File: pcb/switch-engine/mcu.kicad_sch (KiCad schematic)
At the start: 78 parts, among them J10 CORTEX_DEBUG_ETM, J12 CONN_01X03, J13 PMOD_HOST, J26 RJ45, J9 PMOD_HOST, U14 ECS-1612MV-250-CN, U17 AT24MAC402, U29 ADM3101E_QFN, U8 XCKU5P-2FFVB676I, U9 STM32H735-UFBGA176-25

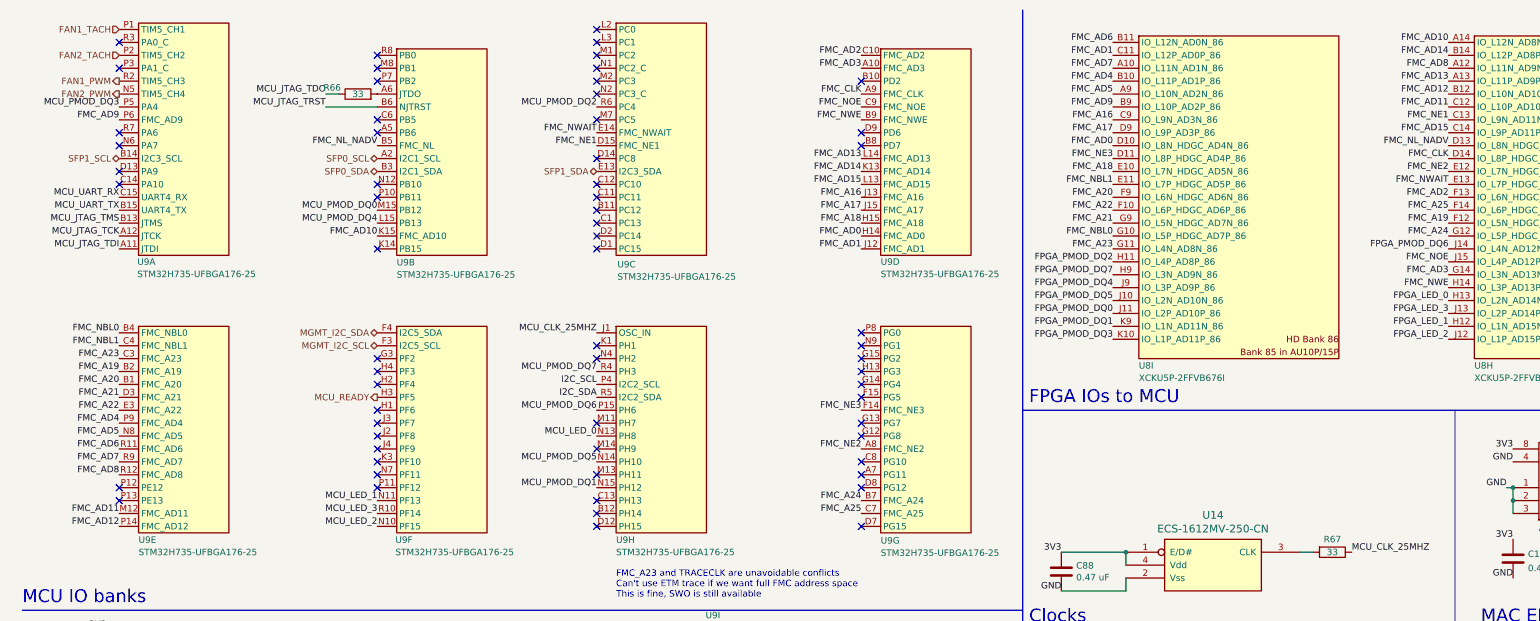
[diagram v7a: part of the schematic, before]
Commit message: Continued layout of MCU area, added cutout for fan
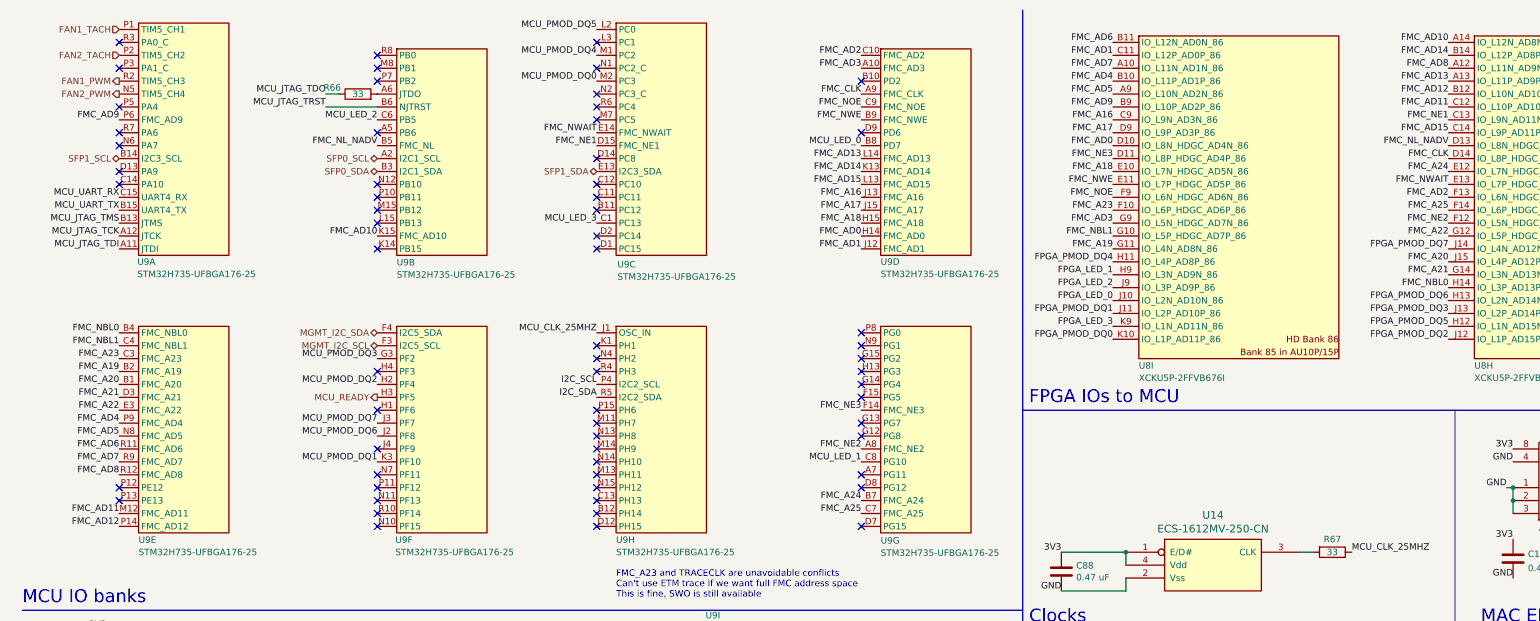
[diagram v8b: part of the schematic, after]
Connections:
- net FMC_A19: now also U8.G11 (IO_L4N_AD8N_86); no longer U8.F12 (IO_L5N_HDGC_87)
- net FMC_A20: now also U8.J15 (IO_L4P_AD12P_87); no longer U8.F9 (IO_L6N_HDGC_AD6N_86)
- net FMC_A21: now also U8.G14 (IO_L3N_AD13N_87); no longer U8.G9 (IO_L5N_HDGC_AD7N_86)
- net FMC_A22: now also U8.G12 (IO_L5P_HDGC_87); no longer U8.F10 (IO_L6P_HDGC_AD6P_86)
- net FMC_A23: now also U8.F10 (IO_L6P_HDGC_AD6P_86); no longer U8.G11 (IO_L4N_AD8N_86)
- net FMC_A24: now also U8.E12 (IO_L7N_HDGC_87); no longer U8.G12 (IO_L5P_HDGC_87)
- net FMC_AD3: now also U8.G9 (IO_L5N_HDGC_AD7N_86); no longer U8.G14 (IO_L3N_AD13N_87)
- net FMC_NBL0: now also U8.H14 (IO_L3P_AD13P_87); no longer U8.G10 (IO_L5P_HDGC_AD7P_86)
- net FMC_NBL1: now also U8.G10 (IO_L5P_HDGC_AD7P_86); no longer U8.E11 (IO_L7P_HDGC_AD5P_86)
- net FMC_NE2: now also U8.F12 (IO_L5N_HDGC_87); no longer U8.E12 (IO_L7N_HDGC_87)
- net FMC_NOE: now also U8.F9 (IO_L6N_HDGC_AD6N_86); no longer U8.J15 (IO_L4P_AD12P_87)
- net FMC_NWE: now also U8.E11 (IO_L7P_HDGC_AD5P_86); no longer U8.H14 (IO_L3P_AD13P_87)
- net FPGA_LED_0: now also U8.J10 (IO_L2N_AD10N_86); no longer U8.H13 (IO_L2N_AD14N_87)
- net FPGA_LED_1: now also U8.H9 (IO_L3N_AD9N_86); no longer U8.H12 (IO_L1N_AD15N_87)
- net FPGA_LED_2: now also U8.J9 (IO_L3P_AD9P_86); no longer U8.J12 (IO_L1P_AD15P_87)
- net FPGA_LED_3: now also U8.K9 (IO_L1N_AD11N_86); no longer U8.J13 (IO_L2P_AD14P_87)
- net FPGA_PMOD_DQ0: now also U8.K10 (IO_L1P_AD11P_86); no longer U8.J11 (IO_L2P_AD10P_86)
- net FPGA_PMOD_DQ1: now also U8.J11 (IO_L2P_AD10P_86); no longer U8.K9 (IO_L1N_AD11N_86)
- net FPGA_PMOD_DQ2: now also U8.J12 (IO_L1P_AD15P_87); no longer U8.H11 (IO_L4P_AD8P_86)
- net FPGA_PMOD_DQ3: now also U8.J13 (IO_L2P_AD14P_87); no longer U8.K10 (IO_L1P_AD11P_86)
- net FPGA_PMOD_DQ4: now also U8.H11 (IO_L4P_AD8P_86); no longer U8.J9 (IO_L3P_AD9P_86)
- net FPGA_PMOD_DQ5: now also U8.H12 (IO_L1N_AD15N_87); no longer U8.J10 (IO_L2N_AD10N_86)
- net FPGA_PMOD_DQ6: now also U8.H13 (IO_L2N_AD14N_87); no longer U8.J14 (IO_L4N_AD12N_87)
- net FPGA_PMOD_DQ7: now also U8.J14 (IO_L4N_AD12N_87); no longer U8.H9 (IO_L3N_AD9N_86)
- net MCU_LED_0: now also U9.B8 (PD7); no longer U9.N13 (PH8)
- net MCU_LED_1: now also U9.C8 (PG10); no longer U9.N11 (PF13)
- net MCU_LED_2: now also U9.C6 (PB5); no longer U9.N10 (PF15)
- net MCU_LED_3: now also U9.C1 (PC13); no longer U9.R10 (PF14)
- net MCU_PMOD_DQ0: now also U9.M2 (PC3); no longer U9.M15 (PB12)
- net MCU_PMOD_DQ1: now also U9.K3 (PF10); no longer U9.N15 (PH12)
- net MCU_PMOD_DQ2: now also U9.H2 (PF4); no longer U9.R6 (PC4)
- net MCU_PMOD_DQ3: now also U9.G3 (PF2); no longer U9.P5 (PA4)
- net MCU_PMOD_DQ4: now also U9.M1 (PC2); no longer U9.L15 (PB13)
- net MCU_PMOD_DQ5: now also U9.L2 (PC0); no longer U9.N14 (PH10)
- net MCU_PMOD_DQ6: now also U9.J2 (PF8); no longer U9.P15 (PH6)
- net MCU_PMOD_DQ7: now also U9.J3 (PF7); no longer U9.R4 (PH3)
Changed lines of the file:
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@@
 	(title_block
 		(title "LATENTRED Ethernet Switch - Main Board")
-		(date "2025-06-04")
+		(date "2025-06-06")
 		(rev "0.1")
 		(company "Antikernel Labs")
@@
 	)
 	(no_connect
-		(at 127 109.22)
+		(at 127 31.75)
 	)
 	(no_connect
-		(at 127 54.61)
+		(at 127 109.22)
 	)
 	(no_connect
@@
 	)
 	(no_connect
-		(at 179.07 101.6)
+		(at 33.02 31.75)
+	)
+	(no_connect
+		(at 127 83.82)
 	)
 	(no_connect
@@
 	)
 	(no_connect
-		(at 83.82 93.98)
-	)
-	(no_connect
 		(at 179.07 114.3)
 	)
@@
 	)
 	(no_connect
-		(at 179.07 39.37)
+		(at 127 96.52)
 	)
 	(no_connect
@@
 	)
 	(no_connect
-		(at 83.82 86.36)
+		(at 83.82 111.76)
+	)
+	(no_connect
+		(at 127 106.68)
 	)
 	(no_connect
@@
 	)
 	(no_connect
-		(at 179.07 86.36)
+		(at 83.82 109.22)
 	)
 	(no_connect
-		(at 83.82 59.69)
+		(at 179.07 86.36)
 	)
 	(no_connect
-		(at 83.82 34.29)
+		(at 83.82 59.69)
 	)
 	(no_connect
@@
 	)
 	(no_connect
-		(at 83.82 81.28)
+		(at 83.82 91.44)
 	)
 	(no_connect
-		(at 127 21.59)
+		(at 179.07 96.52)
 	)
 	(no_connect
-		(at 83.82 91.44)
+		(at 127 101.6)
 	)
 	(no_connect
-		(at 179.07 96.52)
+		(at 83.82 114.3)
 	)
 	(no_connect
@@
 	)
 	(no_connect
+		(at 83.82 54.61)
+	)
+	(no_connect
+		(at 83.82 52.07)
+	)
+	(no_connect
 		(at 127 57.15)
 	)
@@
 	)
 	(no_connect
-		(at 83.82 101.6)
-	)
-	(no_connect
 		(at 83.82 46.99)
 	)
 	(no_connect
-		(at 127 26.67)
-	)
-	(no_connect
 		(at 179.07 81.28)
 	)
@@
 	)
 	(no_connect
+		(at 127 91.44)
+	)
+	(no_connect
 		(at 27.94 261.62)
 	)
@@
 	)
 	(no_connect
-		(at 83.82 96.52)
-	)
-	(no_connect
 		(at 83.82 49.53)
 	)
@@
 	)
 	(no_connect
-		(at 127 16.51)
-	)
-	(no_connect
 		(at 179.07 88.9)
 	)
@@
 	)
 	(label "FPGA_PMOD_DQ6"
-		(at 294.64 59.69 180)
+		(at 294.64 69.85 180)
 		(fields_autoplaced yes)
 		(effects
@@
 	)
 	(label "FMC_AD3"
-		(at 294.64 64.77 180)
+		(at 228.6 54.61 180)
 		(fields_autoplaced yes)
 		(effects
@@
 	)
 	(label "FMC_NWE"
-		(at 294.64 67.31 180)
+		(at 228.6 46.99 180)
 		(fields_autoplaced yes)
 		(effects
@@
 	)
 	(label "MCU_LED_2"
-		(at 83.82 114.3 180)
+		(at 83.82 34.29 180)
 		(fields_autoplaced yes)
 		(effects
@@
 	)
 	(label "MCU_LED_1"
-		(at 83.82 109.22 180)
+		(at 179.07 101.6 180)
 		(fields_autoplaced yes)
 		(effects
@@
 	)
 	(label "FMC_NBL1"
-		(at 228.6 46.99 180)
+		(at 228.6 57.15 180)
 		(fields_autoplaced yes)
 		(effects
@@
 	)
 	(label "FPGA_PMOD_DQ4"
-		(at 228.6 67.31 180)
+		(at 228.6 62.23 180)
 		(fields_autoplaced yes)
 		(effects
@@
 	)
 	(label "FPGA_LED_0"
-		(at 294.64 69.85 180)
+		(at 228.6 69.85 180)
 		(fields_autoplaced yes)
 		(effects
@@
 	)
 	(label "MCU_LED_3"
-		(at 83.82 111.76 180)
+		(at 127 54.61 180)
 		(fields_autoplaced yes)
 		(effects
@@
 	)
 	(label "MCU_PMOD_DQ4"
-		(at 83.82 54.61 180)
+		(at 127 21.59 180)
 		(fields_autoplaced yes)
 		(effects
@@
 	)
 	(label "FPGA_LED_3"
-		(at 294.64 72.39 180)
+		(at 228.6 74.93 180)
 		(fields_autoplaced yes)
 		(effects
@@
 	)
 	(label "MCU_PMOD_DQ6"
-		(at 127 91.44 180)
+		(at 83.82 96.52 180)
 		(fields_autoplaced yes)
 		(effects
@@
 	)
 	(label "FPGA_LED_2"
-		(at 294.64 77.47 180)
+		(at 228.6 67.31 180)
 		(fields_autoplaced yes)
 		(effects
@@
 	)
 	(label "FPGA_LED_1"
-		(at 294.64 74.93 180)
+		(at 228.6 64.77 180)
 		(fields_autoplaced yes)
 		(effects
@@
 	)
 	(label "MCU_LED_0"
-		(at 127 96.52 180)
+		(at 179.07 39.37 180)
 		(fields_autoplaced yes)
 		(effects
@@
 	)
 	(label "MCU_PMOD_DQ2"
-		(at 127 31.75 180)
+		(at 83.82 86.36 180)
 		(fields_autoplaced yes)
 		(effects
@@
 	)
 	(label "FMC_NOE"
-		(at 294.64 62.23 180)
+		(at 228.6 49.53 180)
 		(fields_autoplaced yes)
 		(effects
@@
 	)
 	(label "FMC_A21"
-		(at 228.6 54.61 180)
+		(at 294.64 64.77 180)
 		(fields_autoplaced yes)
 		(effects
@@
 	)
 	(label "FMC_A20"
-		(at 228.6 49.53 180)
+		(at 294.64 62.23 180)
 		(fields_autoplaced yes)
 		(effects
@@
 	)
 	(label "FPGA_PMOD_DQ5"
-		(at 228.6 69.85 180)
+		(at 294.64 74.93 180)
 		(fields_autoplaced yes)
 		(effects
@@
 	)
 	(label "FPGA_PMOD_DQ7"
-		(at 228.6 64.77 180)
+		(at 294.64 59.69 180)
 		(fields_autoplaced yes)
 		(effects
@@
 	)
 	(label "MCU_PMOD_DQ5"
-		(at 127 101.6 180)
+		(at 127 16.51 180)
 		(fields_autoplaced yes)
 		(effects
@@
 	)
 	(label "FMC_A23"
-		(at 228.6 59.69 180)
+		(at 228.6 52.07 180)
 		(fields_autoplaced yes)
 		(effects
@@
 	)
 	(label "MCU_PMOD_DQ7"
-		(at 127 83.82 180)
+		(at 83.82 93.98 180)
 		(fields_autoplaced yes)
 		(effects
@@
 	)
 	(label "FPGA_PMOD_DQ3"
-		(at 228.6 77.47 180)
+		(at 294.64 72.39 180)
 		(fields_autoplaced yes)
 		(effects
@@
 	)
 	(label "FPGA_PMOD_DQ0"
-		(at 228.6 72.39 180)
+		(at 228.6 77.47 180)
 		(fields_autoplaced yes)
 		(effects
@@
 	)
 	(label "FMC_A22"
-		(at 228.6 52.07 180)
+		(at 294.64 57.15 180)
 		(fields_autoplaced yes)
 		(effects
@@
 	)
 	(label "MCU_PMOD_DQ0"
-		(at 83.82 52.07 180)
+		(at 127 26.67 180)
 		(fields_autoplaced yes)
 		(effects
@@
 	)
 	(label "FMC_A24"
-		(at 294.64 57.15 180)
+		(at 294.64 44.45 180)
 		(fields_autoplaced yes)
 		(effects
@@
 	)
 	(label "MCU_PMOD_DQ3"
-		(at 33.02 31.75 180)
+		(at 83.82 81.28 180)
 		(fields_autoplaced yes)
 		(effects
@@
 	)
 	(label "FMC_NBL0"
-		(at 228.6 57.15 180)
+		(at 294.64 67.31 180)
 		(fields_autoplaced yes)
 		(effects
@@
 	)
 	(label "FPGA_PMOD_DQ2"
-		(at 228.6 62.23 180)
+		(at 294.64 77.47 180)
 		(fields_autoplaced yes)
 		(effects
@@
 	)
 	(label "FPGA_PMOD_DQ1"
-		(at 228.6 74.93 180)
+		(at 228.6 72.39 180)
 		(fields_autoplaced yes)
 		(effects
@@
 	)
 	(label "MCU_PMOD_DQ1"
-		(at 127 106.68 180)
+		(at 83.82 101.6 180)
 		(fields_autoplaced yes)
 		(effects
@@
 	)
 	(label "FMC_A19"
-		(at 294.64 54.61 180)
+		(at 228.6 59.69 180)
 		(fields_autoplaced yes)
 		(effects
@@
 	)
 	(label "FMC_NE2"
-		(at 294.64 44.45 180)
+		(at 294.64 54.61 180)
 		(fields_autoplaced yes)
 		(effects
